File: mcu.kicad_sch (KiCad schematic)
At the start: 1 part, among them U1 RP2040

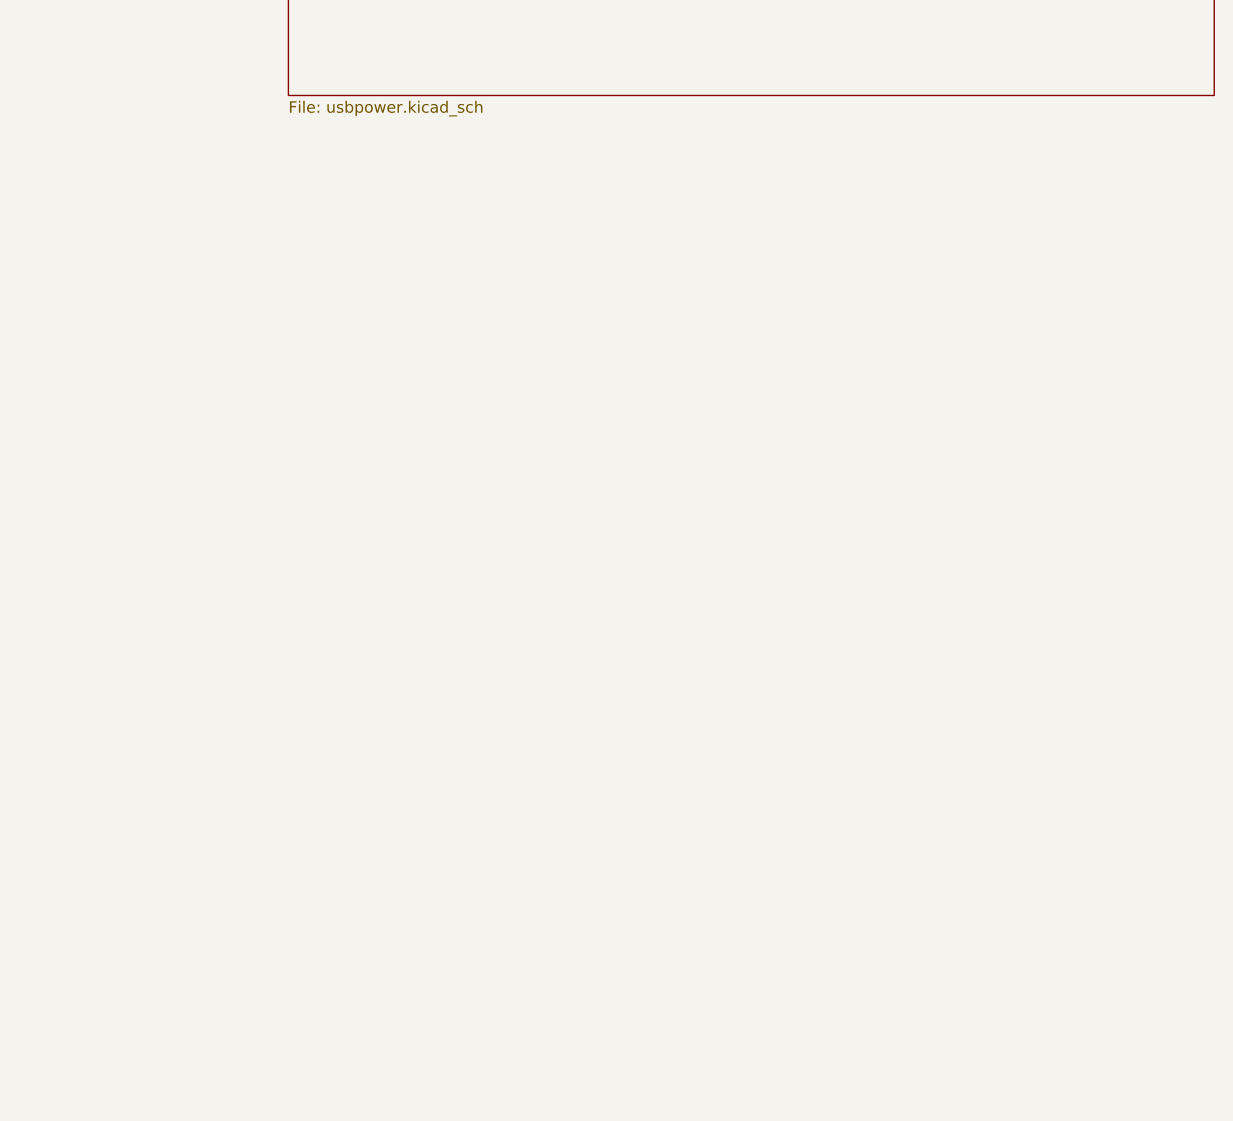
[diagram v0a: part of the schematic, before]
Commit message: added oscillator and memory
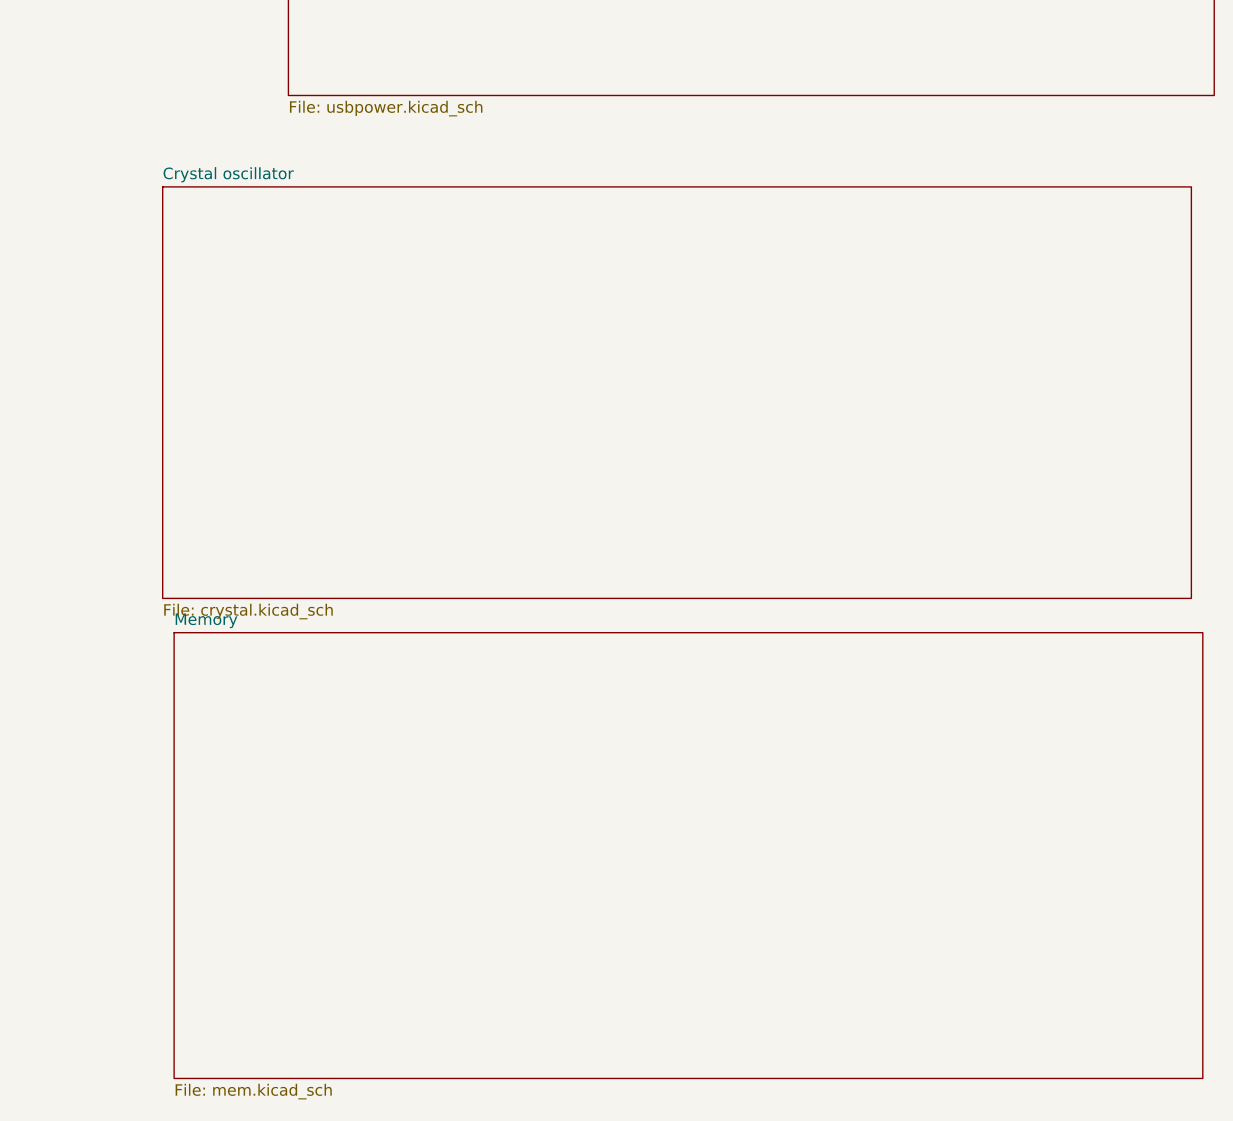
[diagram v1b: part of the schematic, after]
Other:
- added sheet Crystal oscillator (crystal.kicad_sch)
- added sheet Memory (mem.kicad_sch)
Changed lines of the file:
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@@
+	)
+	(sheet
+		(at 168.91 116.84)
+		(size 114.3 49.53)
+		(exclude_from_sim no)
+		(in_bom yes)
+		(on_board yes)
+		(dnp no)
+		(fields_autoplaced yes)
+		(stroke
+			(width 0.1524)
+			(type solid)
+		)
+		(fill
+			(color 0 0 0 0.0000)
+		)
+		(property "Sheetname" "Memory"
+			(at 168.91 116.1284 0)
+			(effects
+				(font
+					(size 1.27 1.27)
+				)
+				(justify left bottom)
+			)
+		)
+		(property "Sheetfile" "mem.kicad_sch"
+			(at 168.91 166.9546 0)
+			(effects
+				(font
+					(size 1.27 1.27)
+				)
+				(justify left top)
+			)
+		)
+		(instances
+			(project "SlashOut"
+				(path "/75d7688f-df99-426a-b593-390936606183/572b8eec-91ac-4047-ae36-918ae2dd5ec4"
+					(page "5")
+				)
+			)
+		)
 	)
 	(sheet
@@
 				)
 			)
+		)
+	)
+	(sheet
+		(at 167.64 67.31)
+		(size 114.3 45.72)
+		(exclude_from_sim no)
+		(in_bom yes)
+		(on_board yes)
+		(dnp no)
+		(fields_autoplaced yes)
+		(stroke
+			(width 0.1524)
+			(type solid)
+		)
+		(fill
+			(color 0 0 0 0.0000)
+		)
+		(property "Sheetname" "Crystal oscillator"
+			(at 167.64 66.5984 0)
+			(effects
+				(font
+					(size 1.27 1.27)
+				)
+				(justify left bottom)
+			)
+		)
+		(property "Sheetfile" "crystal.kicad_sch"
+			(at 167.64 113.6146 0)
+			(effects
+				(font
+					(size 1.27 1.27)
+				)
+				(justify left top)
+			)
+		)
+		(instances
+			(project "SlashOut"
+				(path "/75d7688f-df99-426a-b593-390936606183/572b8eec-91ac-4047-ae36-918ae2dd5ec4"
+					(page "6")
+				)
+			)

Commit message: adding labels and updating PCB
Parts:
- added R3, R4: 27, Resistor_SMD:R_0508_1220Metric, symbol Device:R
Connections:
- net XIN: now reaches U1.20 (XIN)
- net XOUT: now reaches U1.21 (XOUT)
- net at U1.46 (USB_DM): now also R4.1
- net at U1.47 (USB_DP): now also R3.1
- net QSPI_SD3: now reaches U1.51 (QSPI_SD3)
- net QSPI_SCLK: now reaches U1.52 (QSPI_SCLK)
- net QSPI_SD0: now reaches U1.53 (QSPI_SD0)
- net QSPI_SD2: now reaches U1.54 (QSPI_SD2)
- net QSPI_SD1: now reaches U1.55 (QSPI_SD1)
- net QSPI_SS: now reaches U1.56 (QSPI_SS)
- new net USB_D+: R3.2
- new net USB_D-: R4.2

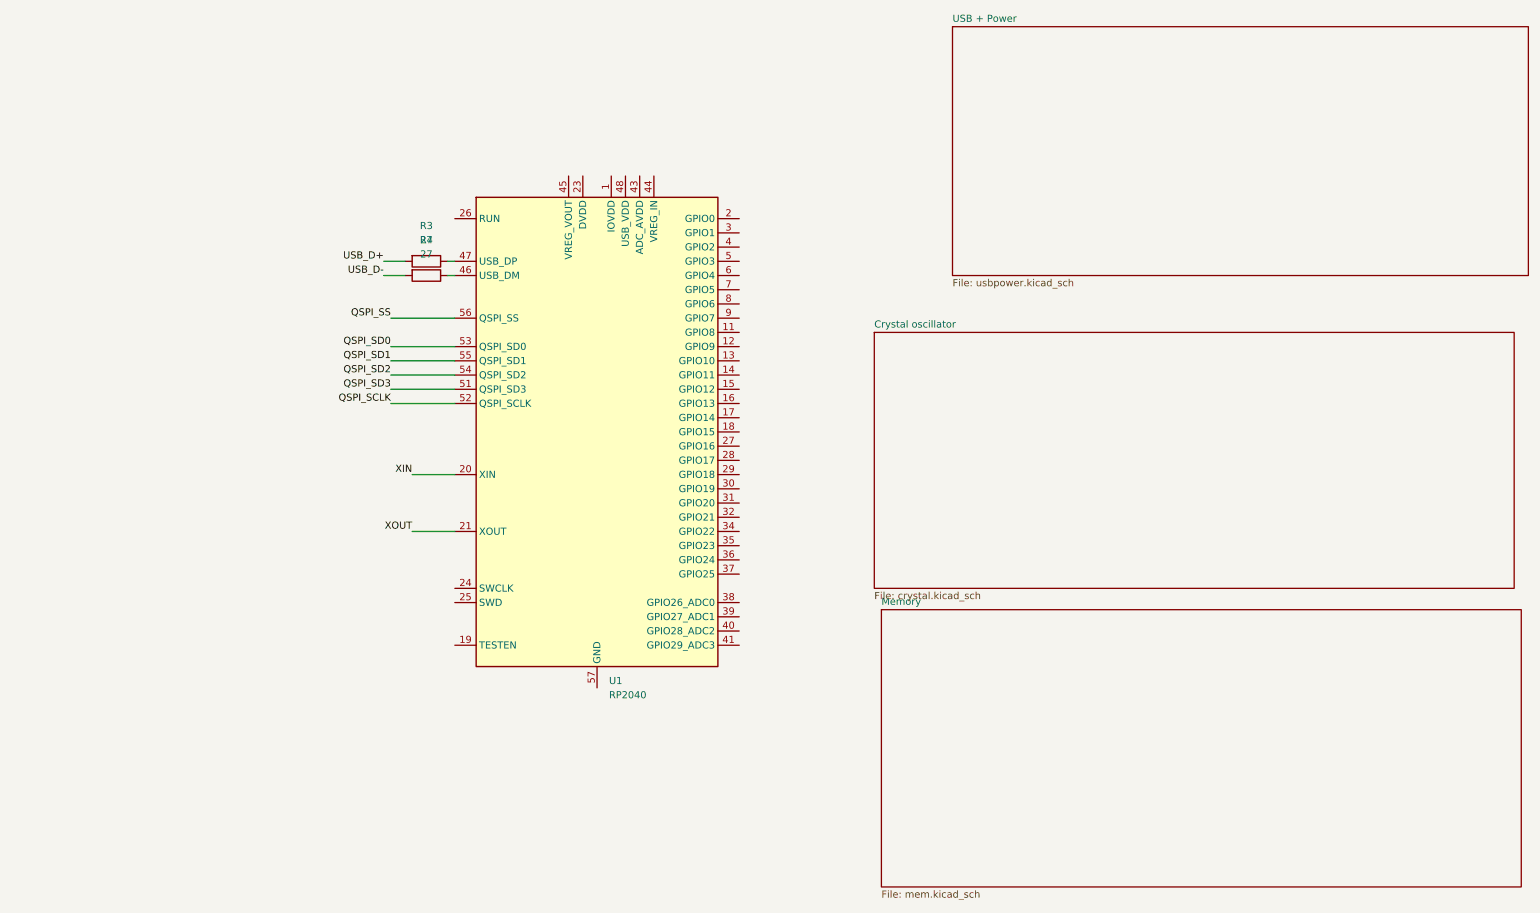
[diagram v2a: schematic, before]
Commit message: Added potentially better Japanese Duplex Matrix
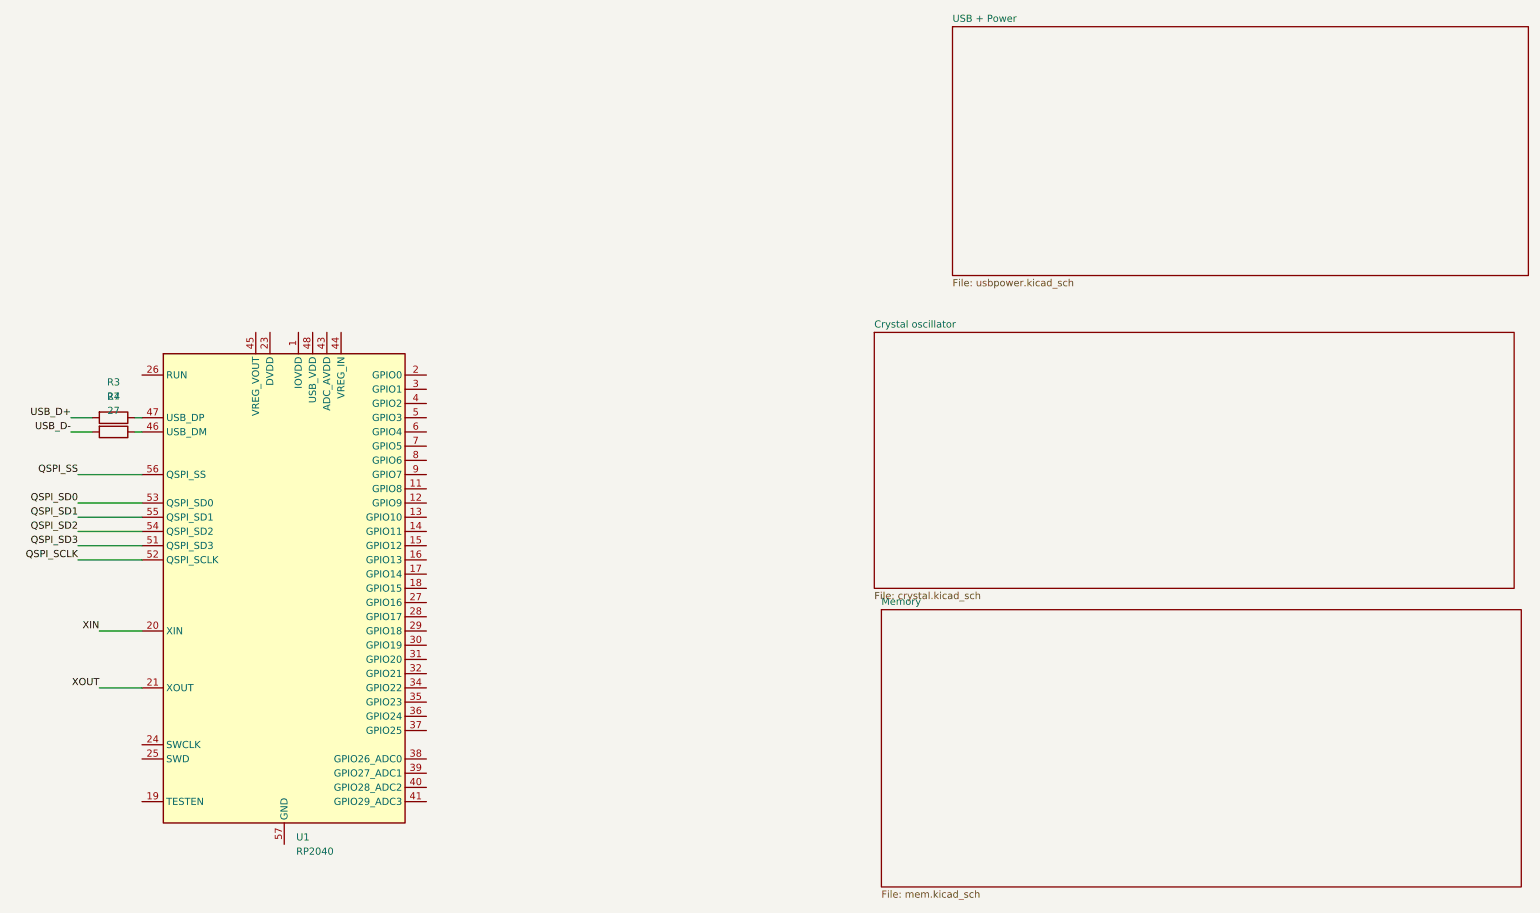
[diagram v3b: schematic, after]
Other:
- moved on the sheet: R3, R4, U1
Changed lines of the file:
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@@
 	(wire
 		(pts
-			(xy 85.09 102.87) (xy 92.71 102.87)
-		)
-		(stroke
-			(width 0)
-			(type default)
-		)
-	)
-	(wire
-		(pts
-			(xy 81.28 74.93) (xy 92.71 74.93)
-		)
-		(stroke
-			(width 0)
-			(type default)
-		)
-	)
-	(wire
-		(pts
-			(xy 91.44 54.61) (xy 92.71 54.61)
-		)
-		(stroke
-			(width 0)
-			(type default)
-		)
-	)
-	(wire
-		(pts
-			(xy 81.28 69.85) (xy 92.71 69.85)
-		)
-		(stroke
-			(width 0)
-			(type default)
-		)
-	)
-	(wire
-		(pts
-			(xy 85.09 92.71) (xy 92.71 92.71)
-		)
-		(stroke
-			(width 0)
-			(type default)
-		)
-	)
-	(wire
-		(pts
-			(xy 91.44 57.15) (xy 92.71 57.15)
-		)
-		(stroke
-			(width 0)
-			(type default)
-		)
-	)
-	(wire
-		(pts
-			(xy 81.28 77.47) (xy 92.71 77.47)
-		)
-		(stroke
-			(width 0)
-			(type default)
-		)
-	)
-	(wire
-		(pts
-			(xy 81.28 64.77) (xy 92.71 64.77)
-		)
-		(stroke
-			(width 0)
-			(type default)
-		)
-	)
-	(wire
-		(pts
-			(xy 80.01 54.61) (xy 83.82 54.61)
-		)
-		(stroke
-			(width 0)
-			(type default)
-		)
-	)
-	(wire
-		(pts
-			(xy 81.28 80.01) (xy 92.71 80.01)
-		)
-		(stroke
-			(width 0)
-			(type default)
-		)
-	)
-	(wire
-		(pts
-			(xy 81.28 72.39) (xy 92.71 72.39)
-		)
-		(stroke
-			(width 0)
-			(type default)
-		)
-	)
-	(wire
-		(pts
-			(xy 80.01 57.15) (xy 83.82 57.15)
+			(xy 29.21 130.81) (xy 36.83 130.81)
+		)
+		(stroke
+			(width 0)
+			(type default)
+		)
+	)
+	(wire
+		(pts
+			(xy 25.4 102.87) (xy 36.83 102.87)
+		)
+		(stroke
+			(width 0)
+			(type default)
+		)
+	)
+	(wire
+		(pts
+			(xy 35.56 82.55) (xy 36.83 82.55)
+		)
+		(stroke
+			(width 0)
+			(type default)
+		)
+	)
+	(wire
+		(pts
+			(xy 25.4 97.79) (xy 36.83 97.79)
+		)
+		(stroke
+			(width 0)
+			(type default)
+		)
+	)
+	(wire
+		(pts
+			(xy 29.21 120.65) (xy 36.83 120.65)
+		)
+		(stroke
+			(width 0)
+			(type default)
+		)
+	)
+	(wire
+		(pts
+			(xy 35.56 85.09) (xy 36.83 85.09)
+		)
+		(stroke
+			(width 0)
+			(type default)
+		)
+	)
+	(wire
+		(pts
+			(xy 25.4 105.41) (xy 36.83 105.41)
+		)
+		(stroke
+			(width 0)
+			(type default)
+		)
+	)
+	(wire
+		(pts
+			(xy 25.4 92.71) (xy 36.83 92.71)
+		)
+		(stroke
+			(width 0)
+			(type default)
+		)
+	)
+	(wire
+		(pts
+			(xy 24.13 82.55) (xy 27.94 82.55)
+		)
+		(stroke
+			(width 0)
+			(type default)
+		)
+	)
+	(wire
+		(pts
+			(xy 25.4 107.95) (xy 36.83 107.95)
+		)
+		(stroke
+			(width 0)
+			(type default)
+		)
+	)
+	(wire
+		(pts
+			(xy 25.4 100.33) (xy 36.83 100.33)
+		)
+		(stroke
+			(width 0)
+			(type default)
+		)
+	)
+	(wire
+		(pts
+			(xy 24.13 85.09) (xy 27.94 85.09)
 		)
 		(stroke
@@
 	)
 	(label "XOUT"
-		(at 85.09 102.87 180)
+		(at 29.21 130.81 180)
 		(effects
 			(font
@@
 	)
 	(label "QSPI_SD0"
-		(at 81.28 69.85 180)
+		(at 25.4 97.79 180)
 		(effects
 			(font
@@
 	)
 	(label "QSPI_SS"
-		(at 81.28 64.77 180)
+		(at 25.4 92.71 180)
 		(effects
 			(font
@@
 	)
 	(label "USB_D+"
-		(at 80.01 54.61 180)
+		(at 24.13 82.55 180)
 		(effects
 			(font
@@
 	)
 	(label "QSPI_SCLK"
-		(at 81.28 80.01 180)
+		(at 25.4 107.95 180)
 		(effects
 			(font
@@
 	)
 	(label "QSPI_SD2"
-		(at 81.28 74.93 180)
+		(at 25.4 102.87 180)
 		(effects
 			(font
@@
 	)
 	(label "QSPI_SD1"
-		(at 81.28 72.39 180)
+		(at 25.4 100.33 180)
 		(effects
 			(font
@@
 	)
 	(label "XIN"
-		(at 85.09 92.71 180)
+		(at 29.21 120.65 180)
 		(effects
 			(font
@@
 	)
 	(label "USB_D-"
-		(at 80.01 57.15 180)
+		(at 24.13 85.09 180)
 		(effects
 			(font
@@
 	)
 	(label "QSPI_SD3"
-		(at 81.28 77.47 180)
+		(at 25.4 105.41 180)
 		(effects
 			(font
@@
 	(symbol
 		(lib_id "Device:R")
-		(at 86.36 58.42 0)
+		(at 30.48 86.36 0)
 		(unit 1)
 		(exclude_from_sim no)
@@
 		(fields_autoplaced yes)
 		(property "Reference" "R4"
-			(at 87.63 50.8 0)
+			(at 31.75 78.74 0)
 			(effects
 				(font
@@
 		)
 		(property "Value" "27"
-			(at 87.63 53.34 0)
+			(at 31.75 81.28 0)
 			(effects
 				(font
@@
 		)
 		(property "Footprint" "Resistor_SMD:R_0508_1220Metric"
-			(at 84.582 58.42 90)
+			(at 28.702 86.36 90)
 			(effects
 				(font
@@
 		)
 		(property "Datasheet" "~"
-			(at 87.63 57.15 90)
+			(at 31.75 85.09 90)
 			(effects
 				(font
@@
 		)
 		(property "Description" "Resistor"
-			(at 86.36 58.42 0)
+			(at 30.48 86.36 0)
 			(effects
 				(font
@@
 	(symbol
 		(lib_id "MCU_RaspberryPi:RP2040")
-		(at 118.11 85.09 0)
+		(at 62.23 113.03 0)
 		(unit 1)
 		(exclude_from_sim no)
@@
 		(fields_autoplaced yes)
 		(property "Reference" "U1"
-			(at 120.2533 129.54 0)
+			(at 64.3733 157.48 0)
 			(effects
 				(font
@@
 		)
 		(property "Value" "RP2040"
-			(at 120.2533 132.08 0)
+			(at 64.3733 160.02 0)
 			(effects
 				(font
@@
 		)
 		(property "Footprint" "Package_DFN_QFN:QFN-56-1EP_7x7mm_P0.4mm_EP3.2x3.2mm"
-			(at 118.11 85.09 0)
+			(at 62.23 113.03 0)
 			(effects
 				(font
@@
 		)
 		(property "Datasheet" "https://datasheets.raspberrypi.com/rp2040/rp2040-datasheet.pdf"
-			(at 118.11 85.09 0)
+			(at 62.23 113.03 0)
 			(effects
 				(font
@@
 		)
 		(property "Description" "A microcontroller by Raspberry Pi"
-			(at 118.11 85.09 0)
+			(at 62.23 113.03 0)
 			(effects
 				(font
@@
 	(symbol
 		(lib_id "Device:R")
-		(at 86.36 55.88 0)
+		(at 30.48 83.82 0)
 		(unit 1)
 		(exclude_from_sim no)
@@
 		(fields_autoplaced yes)
 		(property "Reference" "R3"
-			(at 87.63 48.26 0)
+			(at 31.75 76.2 0)
 			(effects
 				(font
@@
 		)
 		(property "Value" "27"
-			(at 87.63 50.8 0)
+			(at 31.75 78.74 0)
 			(effects
 				(font
@@
 		)
 		(property "Footprint" "Resistor_SMD:R_0508_1220Metric"
-			(at 84.582 55.88 90)
+			(at 28.702 83.82 90)
 			(effects
 				(font
@@
 		)
 		(property "Datasheet" "~"
-			(at 87.63 54.61 90)
+			(at 31.75 82.55 90)
 			(effects
 				(font
@@
 		)
 		(property "Description" "Resistor"
-			(at 86.36 55.88 0)
-			(effects
-				(font
+			(at 30.48 83.82 0)
+			(effects
+				(font
